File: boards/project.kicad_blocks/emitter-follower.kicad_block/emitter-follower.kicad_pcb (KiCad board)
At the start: 2 copper layers, 5 parts, among them Q101 MMBT5401

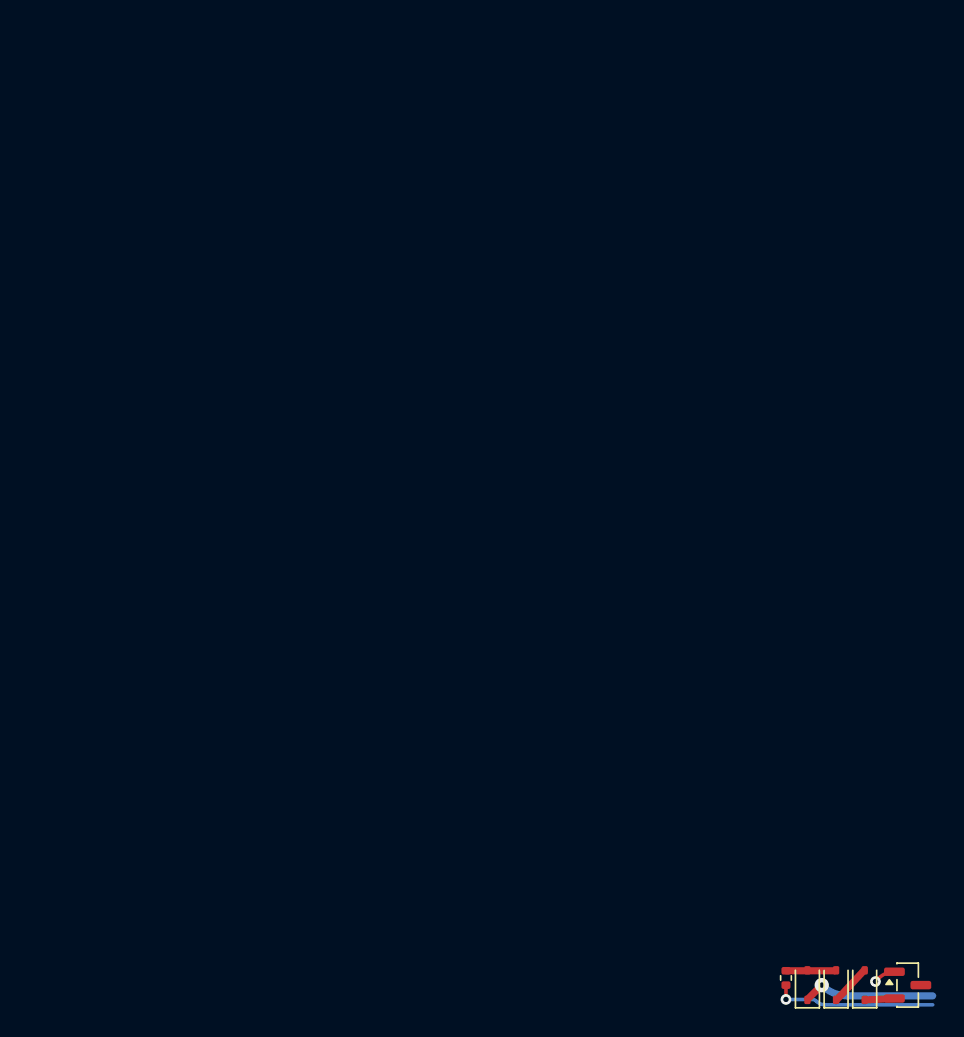
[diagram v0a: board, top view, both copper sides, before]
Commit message: Layout the left three columns.
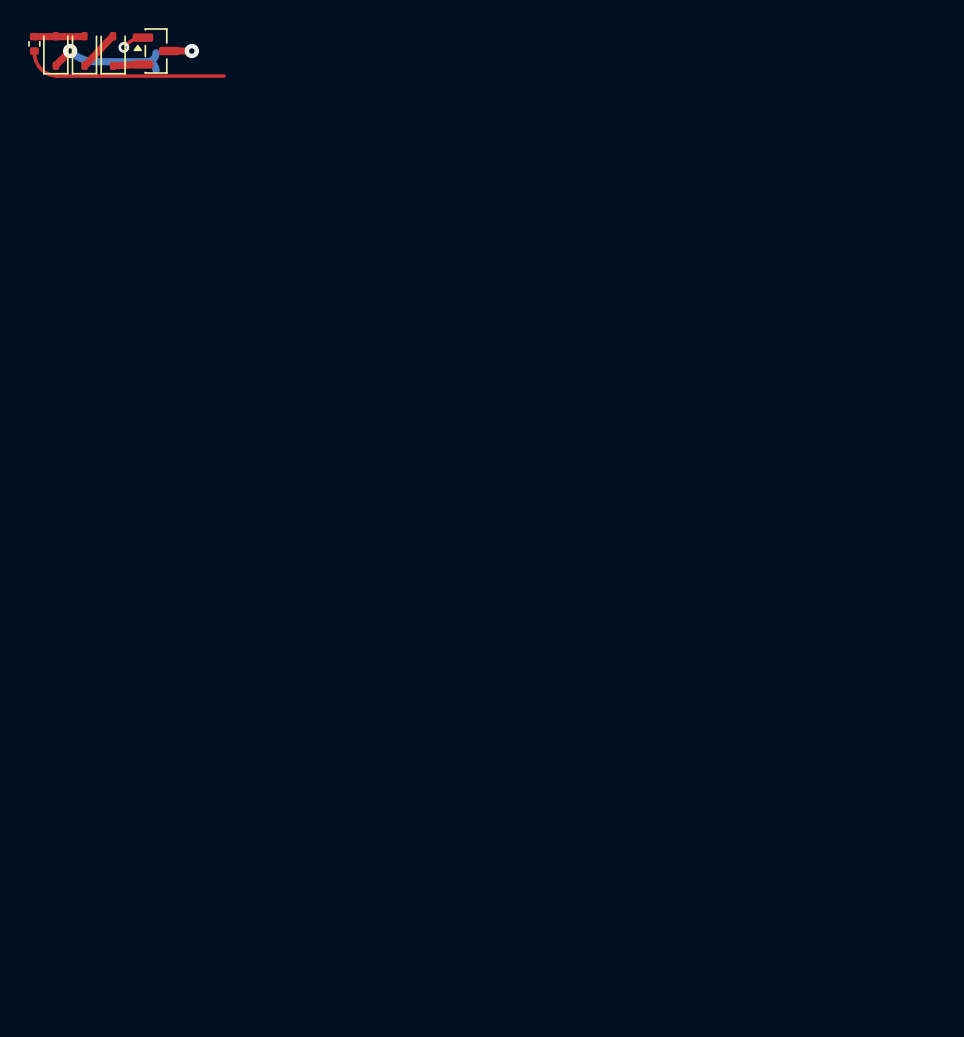
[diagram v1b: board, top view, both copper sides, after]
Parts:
- removed CR21, CR22, CR23: 1N5819WS, Diode_SMD:D_SOD-323
- removed Q101: MMBT5401, Package_TO_SOT_SMD:SOT-23
- removed R499: 56k, Resistor_SMD:R_0402_1005Metric
- added CR11: 1N4148WS, Diode_SMD:D_SOD-323, F.Cu at (118.9, 88.1)
- added CR12: 1N4148WS, Diode_SMD:D_SOD-323, F.Cu at (120.9, 88.1)
- added CR13: 1N4148WS, Diode_SMD:D_SOD-323, F.Cu at (122.9, 88.1)
- added Q26: MMBT5401, Package_TO_SOT_SMD:SOT-23, F.Cu at (126.0, 88.1)
- added R200: 56k, Resistor_SMD:R_0402_1005Metric, F.Cu at (117.3, 87.6)
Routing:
- net ~{Q3}: track 3.48 -> 0.00 mm
- net ~{G}: track 0.00 -> 3.48 mm
- net +15V: track 11.5 -> 14.5 mm, vias 1 -> 0
- net Net-(CR12-K): track 0.00 -> 2.87 mm
- net Net-(CR22-K): track 2.87 -> 0.00 mm
- net Net-(CR23-K): track 2.07 -> 0.00 mm
- net Net-(CR13-K): track 0.00 -> 2.07 mm
- net -15V: track 0.00 -> 1.60 mm, vias 0 -> 1
- net /Q3/~{Q3_{S}}: track 1.56 -> 0.00 mm, vias 1 -> 0
- net /G Flip-Flop/~{G_{S}}: track 0.00 -> 1.56 mm, vias 0 -> 1
